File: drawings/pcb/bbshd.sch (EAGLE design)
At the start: 58 parts, among them IC1 LM358D

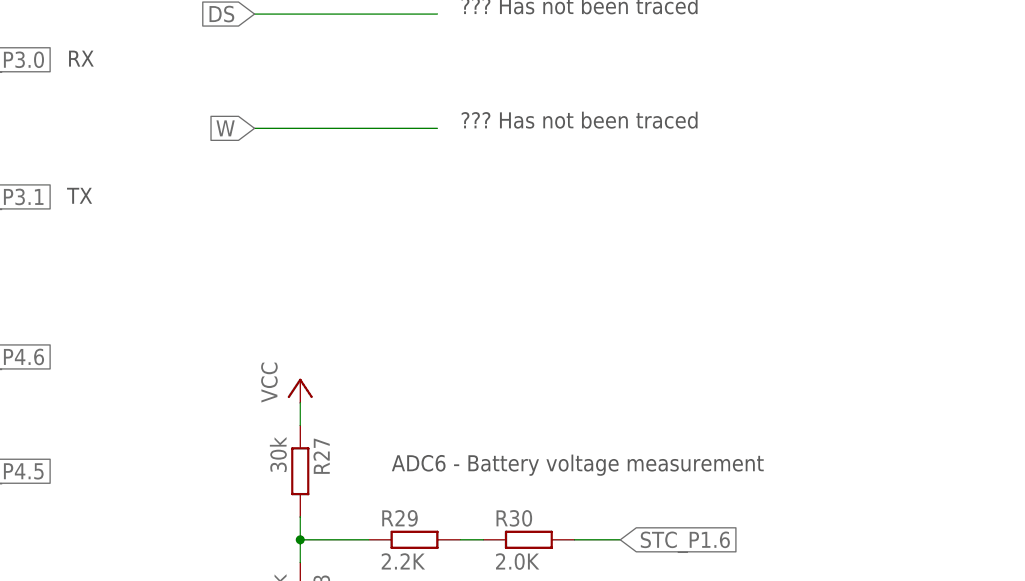
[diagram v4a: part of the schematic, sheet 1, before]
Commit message: add temperature sensor circuit to drawing and implemented rough function for reading controller temperature
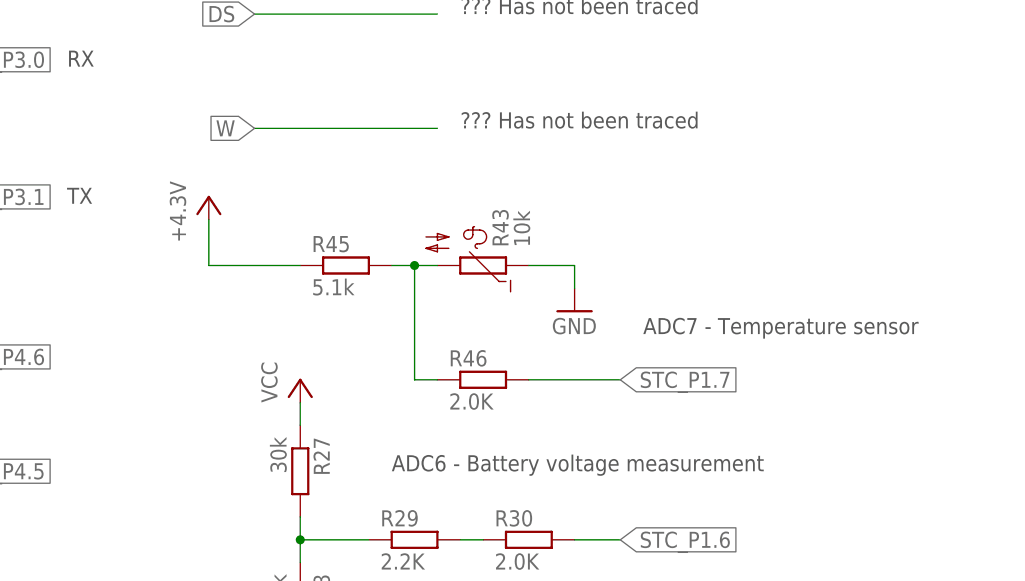
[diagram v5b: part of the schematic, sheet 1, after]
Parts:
- added R43: 10k, ptc-ntc:NTC640
- added R45: 5.1k, rcl:R-EU_R0603
- added R46: 2.0K, rcl:R-EU_R0603
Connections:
- new net N$21: R43.2, R45.2, R46.1
- new net STC_P1.7: R46.2
- net +3V3: now also R45.1
- net GND: now also R43.1
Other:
- note added: "ADC7 - Temperature sensor"
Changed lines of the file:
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@@
 <part name="R20" library="rcl" deviceset="R-EU_" device="R0603" value="0"/>
 <part name="R44" library="rcl" deviceset="R-EU_" device="R0603" value="0"/>
+<part name="R43" library="ptc-ntc" deviceset="NTC640" device="" value="10k"/>
+<part name="R45" library="rcl" deviceset="R-EU_" device="R0603" value="5.1k"/>
+<part name="+3V4" library="supply1" deviceset="+3V3" device="" value="+4.3V"/>
+<part name="GND12" library="supply1" deviceset="GND" device=""/>
+<part name="R46" library="rcl" deviceset="R-EU_" device="R0603" value="2.0K"/>
 </parts>
 <sheets>
@@
 <text x="231.648" y="149.098" size="1.778" layer="97">TxD3</text>
 <text x="161.036" y="139.954" size="1.778" layer="97">Another UART brought out to pins, no data has been seen.</text>
+<text x="208.28" y="71.12" size="1.778" layer="97">ADC7 - Temperature sensor</text>
 </plain>
 <instances>
@@
 <instance part="R41" gate="G$1" x="208.28" y="149.86" rot="R180"/>
 <instance part="R42" gate="G$1" x="208.28" y="124.46" rot="R180"/>
+<instance part="R43" gate="1" x="190.5" y="78.74" rot="R90"/>
+<instance part="R45" gate="G$1" x="175.26" y="78.74"/>
+<instance part="+3V4" gate="G$1" x="160.02" y="86.36"/>
+<instance part="GND12" gate="1" x="200.66" y="73.66"/>
+<instance part="R46" gate="G$1" x="190.5" y="66.04"/>
 </instances>
 <busses>
@@
 <pinref part="GND8" gate="1" pin="GND"/>
 <wire x1="170.18" y1="35.56" x2="170.18" y2="33.02" width="0.1524" layer="91"/>
+</segment>
+<segment>
+<pinref part="R43" gate="1" pin="1"/>
+<wire x1="195.58" y1="78.74" x2="200.66" y2="78.74" width="0.1524" layer="91"/>
+<pinref part="GND12" gate="1" pin="GND"/>
+<wire x1="200.66" y1="78.74" x2="200.66" y2="76.2" width="0.1524" layer="91"/>
 </segment>
 </net>
@@
 <junction x="38.1" y="38.1"/>
 </segment>
+<segment>
+<pinref part="+3V4" gate="G$1" pin="+3V3"/>
+<wire x1="160.02" y1="83.82" x2="160.02" y2="78.74" width="0.1524" layer="91"/>
+<pinref part="R45" gate="G$1" pin="1"/>
+<wire x1="160.02" y1="78.74" x2="170.18" y2="78.74" width="0.1524" layer="91"/>
+</segment>
 </net>
 <net name="N$7" class="0">
@@
 </segment>
 </net>
+<net name="N$21" class="0">
+<segment>
+<pinref part="R45" gate="G$1" pin="2"/>
+<pinref part="R43" gate="1" pin="2"/>
+<wire x1="180.34" y1="78.74" x2="182.88" y2="78.74" width="0.1524" layer="91"/>
+<wire x1="182.88" y1="78.74" x2="185.42" y2="78.74" width="0.1524" layer="91"/>
+<wire x1="182.88" y1="78.74" x2="182.88" y2="66.04" width="0.1524" layer="91"/>
+<junction x="182.88" y="78.74"/>
+<pinref part="R46" gate="G$1" pin="1"/>
+<wire x1="182.88" y1="66.04" x2="185.42" y2="66.04" width="0.1524" layer="91"/>
+</segment>
+</net>
+<net name="STC_P1.7" class="0">
+<segment>
+<pinref part="R46" gate="G$1" pin="2"/>
+<wire x1="195.58" y1="66.04" x2="205.74" y2="66.04" width="0.1524" layer="91"/>
+<label x="205.74" y="66.04" size="1.778" layer="95" xref="yes"/>
+</segment>
+</net>

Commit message: Support motor winding temperature sensor (#45, #46) * Use max value of controller and motor temperature for thermal limiting.
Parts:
- added R47: 5.1K, rcl:R-EU_R0603
- added R48: 10K, ptc-ntc:NTC642-6
- R46: value 2.0K -> 3.0K
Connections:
- net +3V3: no longer R45.1
- net +5V: now also R45.1, R47.1
- net GND: now also R48.2
- net N$16: now also R47.2, R48.1
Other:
- note added: "Components missing, located on the bottom side of pcb right under STC MCU. Two SOT-23, likely two transistors, some form of input protection maybe?"
- note added: "Motor winding temperature sensor. Labeled as "T" on hall sensor board."
- note added: "WARNING: Not sure this opamp circuit is 100% correct, it looks a bit strange. OPAMP is there to amplify voltage drop over shunt resistors in order to get a more detailed reading with ADC."
- note removed: "Components missing, located on the bottom side of pcb right under STC MCU. Two SOT-23, likely two transistors, some form of level conversion to 5V maybe?"
- note removed: "Unknown function (ADC4) Labeled as "T" on hall sensor board. Motor temperature sensor?"
- note removed: "WARNING: Not sure this opamp circuit is 100% correct. OPAMP is there to amplify voltage drop over shunt resistors in order to get a more detailed reading with ADC. Connected to NEC MCU which cannot be programmed atm so doesn't really matter."
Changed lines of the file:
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@@
 <part name="R43" library="ptc-ntc" deviceset="NTC640" device="" value="10k"/>
 <part name="R45" library="rcl" deviceset="R-EU_" device="R0603" value="5.1k"/>
-<part name="+3V4" library="supply1" deviceset="+3V3" device="" value="+4.3V"/>
 <part name="GND12" library="supply1" deviceset="GND" device=""/>
-<part name="R46" library="rcl" deviceset="R-EU_" device="R0603" value="2.0K"/>
+<part name="R46" library="rcl" deviceset="R-EU_" device="R0603" value="3.0K"/>
+<part name="P+8" library="supply1" deviceset="+5V" device=""/>
+<part name="R47" library="rcl" deviceset="R-EU_" device="R0603" value="5.1K"/>
+<part name="P+9" library="supply1" deviceset="+5V" device=""/>
+<part name="R48" library="ptc-ntc" deviceset="NTC642-6" device="" value="10K"/>
+<part name="GND13" library="supply1" deviceset="GND" device=""/>
 </parts>
 <sheets>
@@
 the bottom side of pcb right under STC MCU.
 Two SOT-23, likely two transistors,
-some form of level conversion to 5V maybe?</text>
+some form of input protection maybe?</text>
 <text x="17.018" y="60.198" size="1.778" layer="97">PAS1</text>
 <text x="17.018" y="62.738" size="1.778" layer="97">PAS2</text>
@@
 <instance part="R43" gate="1" x="190.5" y="78.74" rot="R90"/>
 <instance part="R45" gate="G$1" x="175.26" y="78.74"/>
-<instance part="+3V4" gate="G$1" x="160.02" y="86.36"/>
 <instance part="GND12" gate="1" x="200.66" y="73.66"/>
 <instance part="R46" gate="G$1" x="190.5" y="66.04"/>
+<instance part="P+9" gate="1" x="160.02" y="86.36"/>
 </instances>
 <busses>
@@
 <pinref part="D5" gate="G$1" pin="A"/>
 <wire x1="55.88" y1="119.38" x2="55.88" y2="111.76" width="0.1524" layer="91"/>
+</segment>
+<segment>
+<pinref part="R45" gate="G$1" pin="1"/>
+<wire x1="160.02" y1="78.74" x2="170.18" y2="78.74" width="0.1524" layer="91"/>
+<pinref part="P+9" gate="1" pin="+5V"/>
+<wire x1="160.02" y1="83.82" x2="160.02" y2="78.74" width="0.1524" layer="91"/>
 </segment>
 </net>
@@
 <wire x1="43.18" y1="38.1" x2="38.1" y2="38.1" width="0.1524" layer="91"/>
 <junction x="38.1" y="38.1"/>
-</segment>
-<segment>
-<pinref part="+3V4" gate="G$1" pin="+3V3"/>
-<wire x1="160.02" y1="83.82" x2="160.02" y2="78.74" width="0.1524" layer="91"/>
-<pinref part="R45" gate="G$1" pin="1"/>
-<wire x1="160.02" y1="78.74" x2="170.18" y2="78.74" width="0.1524" layer="91"/>
 </segment>
 </net>
@@
 <text x="217.17" y="20.32" size="2.54" layer="94">Daniel Nilsson</text>
 <text x="142.24" y="58.42" size="1.778" layer="97">WARNING:
-Not sure this opamp circuit is 100% correct.
+Not sure this opamp circuit is 100% correct, it looks a bit strange.
 OPAMP is there to amplify voltage drop over shunt
-resistors in order to get a more detailed reading with ADC.
-Connected to NEC MCU which cannot be programmed
-atm so doesn't really matter.</text>
-<text x="68.072" y="166.878" size="1.778" layer="97">Unknown function (ADC4)
-Labeled as "T" on hall sensor board.
-Motor temperature sensor?</text>
+resistors in order to get a more detailed reading with ADC.</text>
+<text x="80.772" y="166.878" size="1.778" layer="97">Motor winding temperature sensor.
+Labeled as "T" on hall sensor board.</text>
 <text x="165.1" y="127" size="1.778" layer="97">Some form of status LED.
 Seems to be blinking during normal operation.</text>
@@
 <instance part="R20" gate="G$1" x="66.04" y="104.14"/>
 <instance part="R44" gate="G$1" x="66.04" y="111.76"/>
+<instance part="P+8" gate="1" x="35.56" y="172.72"/>
+<instance part="R47" gate="G$1" x="43.18" y="165.1"/>
+<instance part="R48" gate="1" x="35.56" y="152.4"/>
+<instance part="GND13" gate="1" x="27.94" y="154.94"/>
 </instances>
 <busses>
@@
 <pinref part="C4" gate="G$1" pin="2"/>
 <wire x1="66.04" y1="152.4" x2="66.04" y2="154.94" width="0.1524" layer="91"/>
+</segment>
+<segment>
+<pinref part="R48" gate="1" pin="2"/>
+<wire x1="35.56" y1="157.48" x2="35.56" y2="160.02" width="0.1524" layer="91"/>
+<wire x1="35.56" y1="160.02" x2="27.94" y2="160.02" width="0.1524" layer="91"/>
+<pinref part="GND13" gate="1" pin="GND"/>
+<wire x1="27.94" y1="160.02" x2="27.94" y2="157.48" width="0.1524" layer="91"/>
 </segment>
 </net>
@@
 <segment>
 <pinref part="JP4" gate="A" pin="6"/>
-<wire x1="27.94" y1="144.78" x2="50.8" y2="144.78" width="0.1524" layer="91"/>
+<wire x1="27.94" y1="144.78" x2="35.56" y2="144.78" width="0.1524" layer="91"/>
+<wire x1="35.56" y1="144.78" x2="50.8" y2="144.78" width="0.1524" layer="91"/>
 <wire x1="50.8" y1="144.78" x2="50.8" y2="165.1" width="0.1524" layer="91"/>
 <pinref part="R39" gate="G$1" pin="1"/>
 <wire x1="50.8" y1="165.1" x2="53.34" y2="165.1" width="0.1524" layer="91"/>
+<pinref part="R47" gate="G$1" pin="2"/>
+<wire x1="48.26" y1="165.1" x2="50.8" y2="165.1" width="0.1524" layer="91"/>
+<junction x="50.8" y="165.1"/>
+<pinref part="R48" gate="1" pin="1"/>
+<wire x1="35.56" y1="147.32" x2="35.56" y2="144.78" width="0.1524" layer="91"/>
+<junction x="35.56" y="144.78"/>
 </segment>
 </net>
@@
 <wire x1="154.94" y1="119.38" x2="162.56" y2="119.38" width="0.1524" layer="91"/>
 </segment>
-</net>
+<segment>
+<pinref part="P+8" gate="1" pin="+5V"/>
+<wire x1="35.56" y1="170.18" x2="35.56" y2="165.1" width="0.1524" layer="91"/>
+<pinref part="R47" gate="G$1" pin="1"/>
+<wire x1="35.56" y1="165.1" x2="38.1" y2="165.1" width="0.1524" layer="91"/>
+</segment>
+</net>

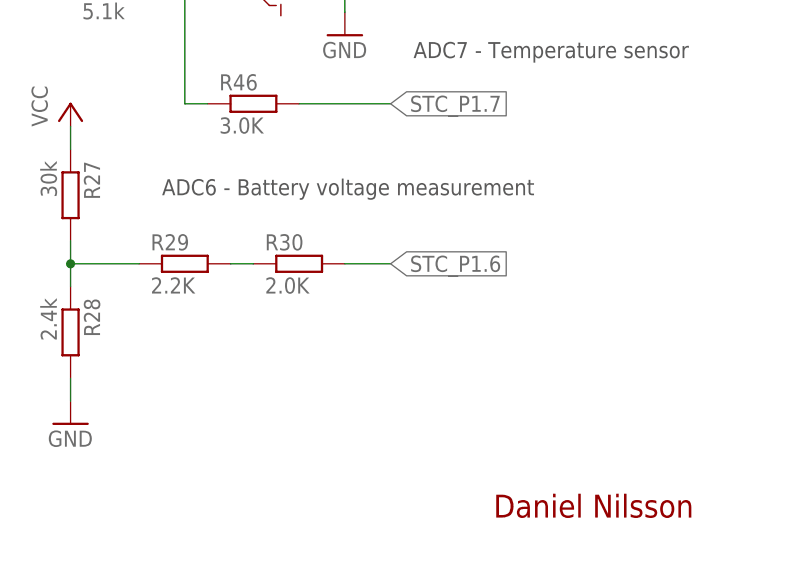
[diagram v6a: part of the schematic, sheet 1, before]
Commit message: ADC voltage reading adjustments * Trace and add voltage reading to NEC MCU in drawing. * Set unused voltage reading pin on STC MCU to input high impedance to not affect reading by NEC MCU. * Set ADC steps per volt to 14.9 which seems to more closely match most BBSHD controllers (will differ between controllers!) * Add voltage reading print to event log.
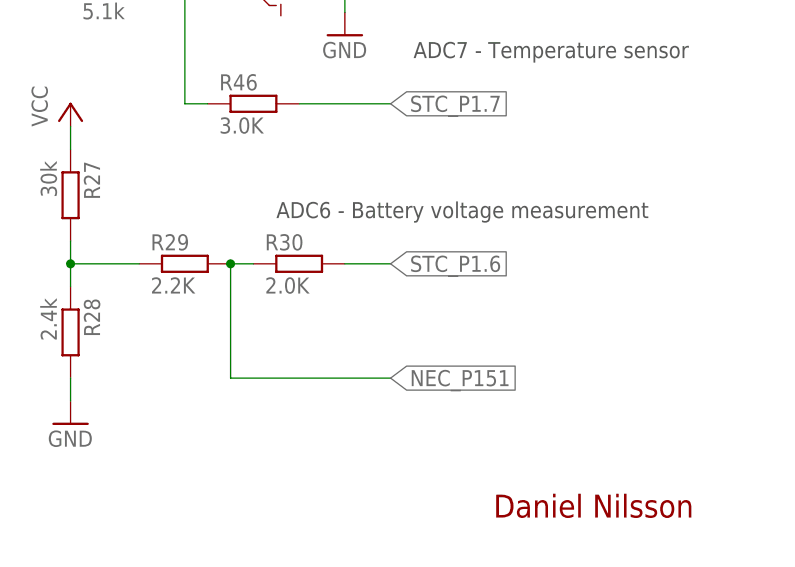
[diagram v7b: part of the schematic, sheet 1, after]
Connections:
- net N$15 renamed NEC_P151
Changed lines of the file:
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@@
 <text x="18.796" y="29.718" size="1.778" layer="97">SPD</text>
 <text x="217.17" y="20.066" size="2.54" layer="94">Daniel Nilsson</text>
-<text x="180.34" y="55.88" size="1.778" layer="97">ADC6 - Battery voltage measurement</text>
+<text x="193.04" y="53.34" size="1.778" layer="97">ADC6 - Battery voltage measurement</text>
 <text x="231.648" y="123.698" size="1.778" layer="97">TxD4</text>
 <text x="231.648" y="133.858" size="1.778" layer="97">RxD4</text>
@@
 </segment>
 </net>
-<net name="N$15" class="0">
+<net name="NEC_P151" class="0">
 <segment>
 <pinref part="R30" gate="G$1" pin="1"/>
 <pinref part="R29" gate="G$1" pin="2"/>
 <wire x1="190.5" y1="48.26" x2="187.96" y2="48.26" width="0.1524" layer="91"/>
-</segment>
-</net>
+<wire x1="187.96" y1="48.26" x2="187.96" y2="35.56" width="0.1524" layer="91"/>
+<junction x="187.96" y="48.26"/>
+<wire x1="187.96" y1="35.56" x2="205.74" y2="35.56" width="0.1524" layer="91"/>
+<label x="205.74" y="35.56" size="1.778" layer="95" xref="yes"/>
+</segment>
+</net>
